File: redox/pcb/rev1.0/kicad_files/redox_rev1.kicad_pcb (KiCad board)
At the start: 2 copper layers, 162.2 x 126.5 mm, 86 parts, among them K0 KEYSW, K1 KEYSW, K10 KEYSW, K11 KEYSW, K12 KEYSW, K13 KEYSW, K14 KEYSW, K15 KEYSW, K16 KEYSW, K2 KEYSW, K20 KEYSW, K21 KEYSW, K22 KEYSW, K23 KEYSW, K24 KEYSW, K25 KEYSW, K26 KEYSW, K3 KEYSW, K30 KEYSW, K31 KEYSW, K32 KEYSW, K33 KEYSW, K34 KEYSW, K35 KEYSW, K36 KEYSW, K4 KEYSW, K40 KEYSW, K41 KEYSW, K42 KEYSW, K43 KEYSW, K44 KEYSW, K45 KEYSW, K46 KEYSW, K5 KEYSW, K6 KEYSW, U1 ProMicro

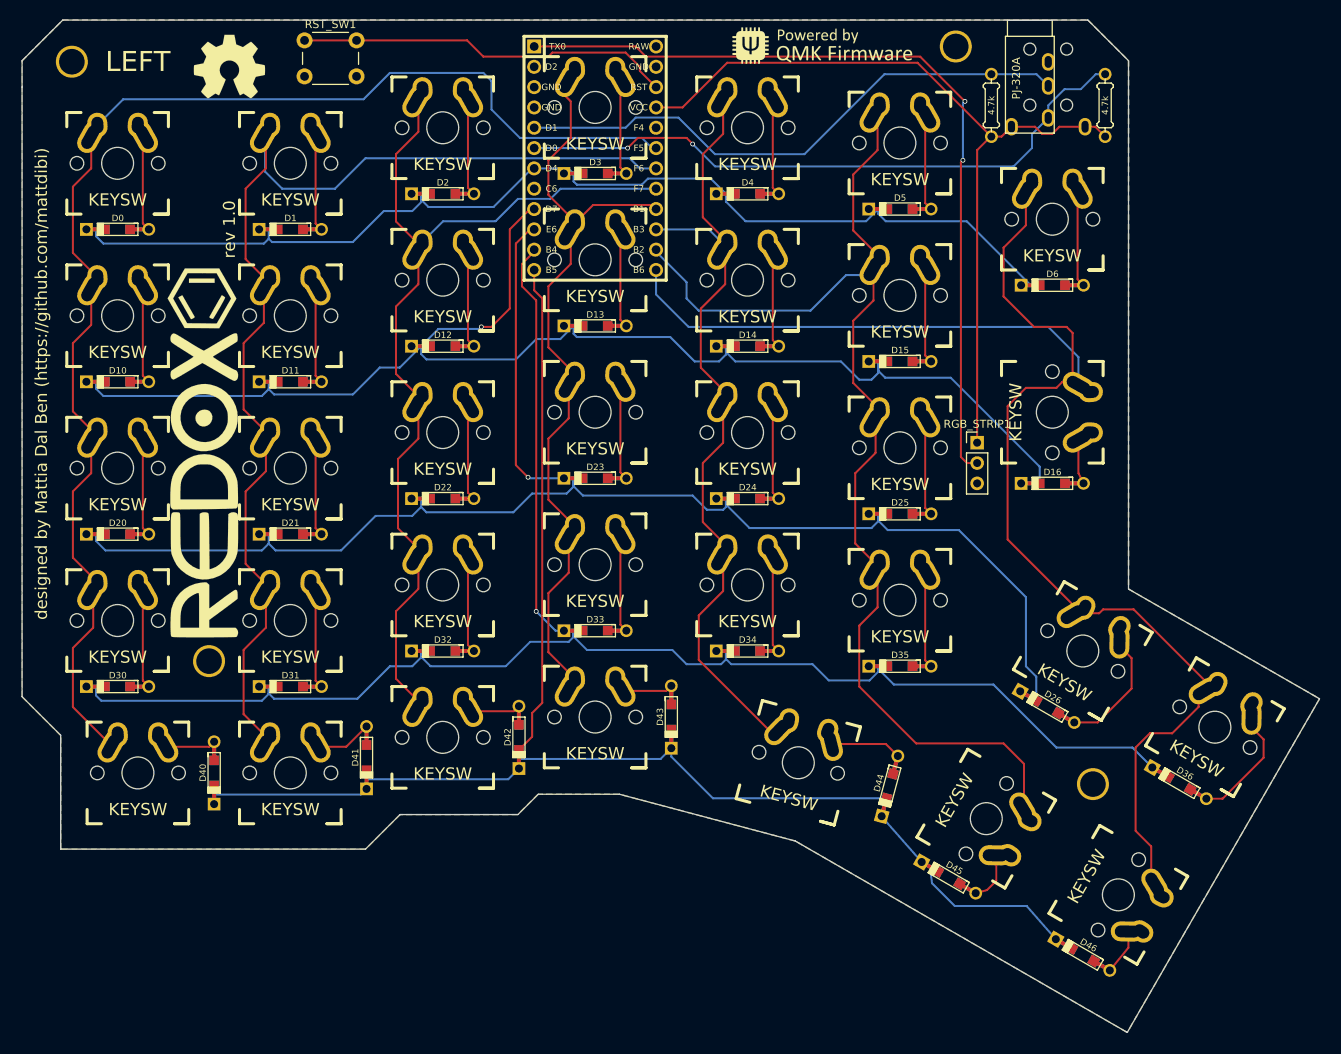
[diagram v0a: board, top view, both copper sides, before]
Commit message: Update to reversible kailh hotswap
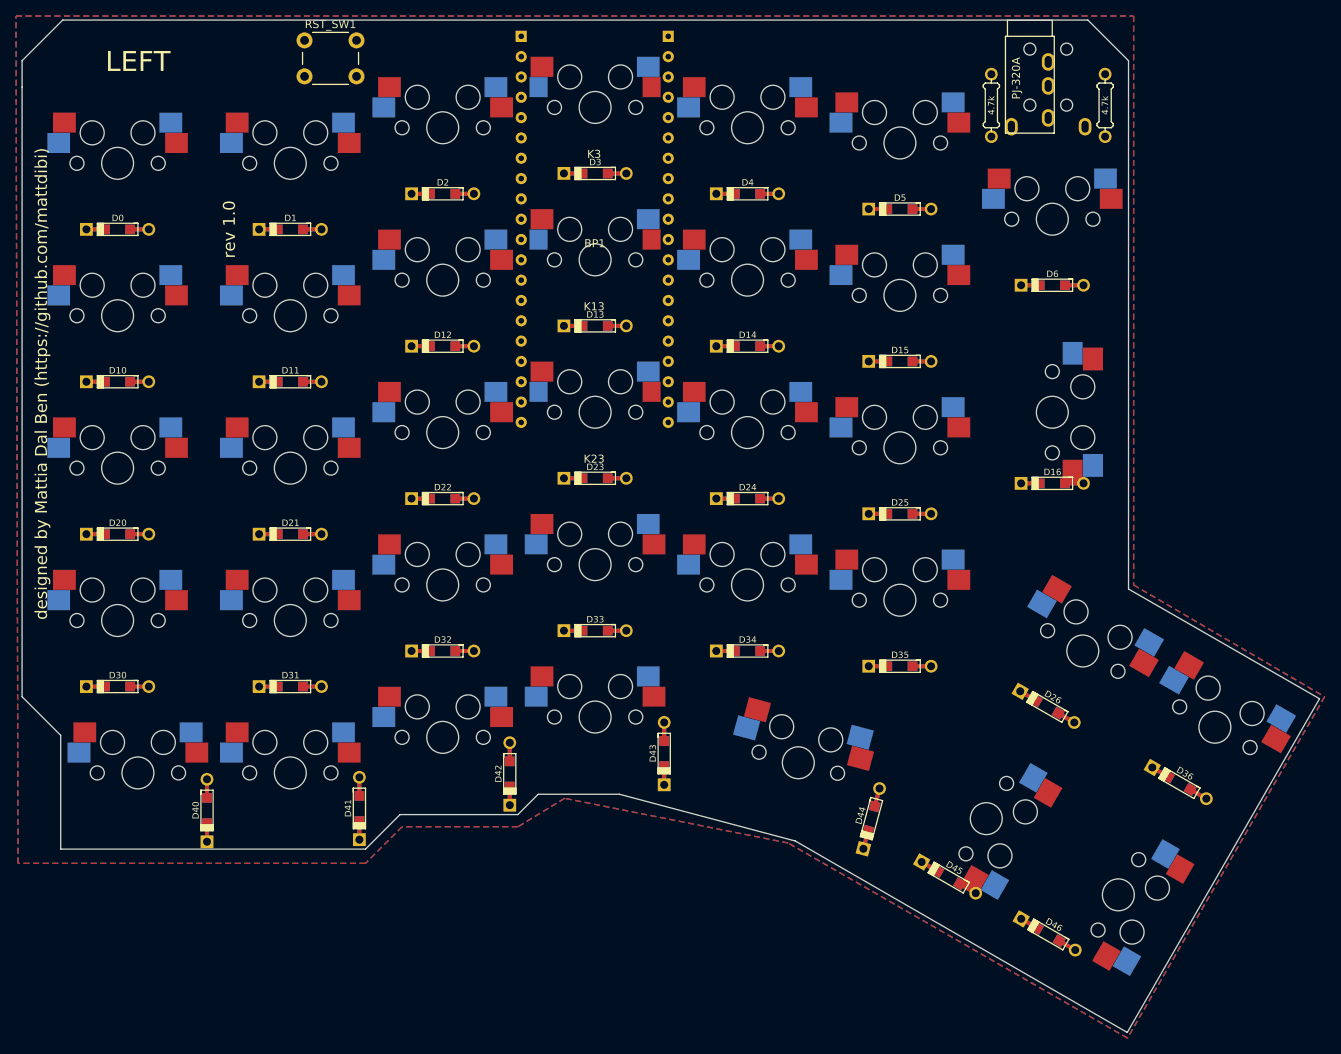
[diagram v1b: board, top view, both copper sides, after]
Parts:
- removed G*** (x2): LOGO, myparts:redox-logo
- removed G*** (x2): LOGO, myparts:qmk-badge
- removed HOLE_M3 (x4): VAL**, keyboard_parts:HOLE_M3
- removed REF*** (x2): OSHW-Logo2_14.6x12mm_SilkScreen, Symbols:OSHW-Symbol_8.9x8mm_SilkScreen
- removed RGB_STRIP1: Conn_01x03, Pin_Headers:Pin_Header_Straight_1x03_Pitch2.54mm
- removed U1: ProMicro, Keebio-Parts:ArduinoProMicro
- added BP1: BlackPill2, reversable_hotswap:BlackPill, F.Cu at (151.1, 76.2)
- K0, K10, K20, K30, K44: footprint myparts:Mx_Alps_125-dualside -> reversable_hotswap:MXOnly-1.25U-Hotswap
- K1, K11, K12, K14, K15, K2, K21, K22, K24, K25, K26, K31, K32, K33, K34, K35, K36, K4, K40, K41, K42, K43, K5, K6: footprint canadian_footprints:Mx_Alps_100-dualside -> reversable_hotswap:MXOnly-1U-Hotswap
- K13, K23, K3: footprint canadian_footprints:Mx_Alps_100-dualside -> reversable_hotswap:MXOnly-1U-Hotswap-Small
- K16, K45, K46: footprint canadian_footprints:Mx_Alps_150-dualsided -> reversable_hotswap:MXOnly-1.5U-Hotswap
- moved D41 6.41 mm to (121.7, 147.3)
- moved D46 5.01 mm to (207.8, 163.1)
- moved D40 4.78 mm to (102.6, 147.6)
- moved D42 4.71 mm to (140.5, 143.0)
- moved D44 4.66 mm to (185.7, 148.6)
- moved D43 4.66 mm to (159.8, 140.5)
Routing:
- net row3: track 207.9 -> 0.00 mm, vias 1 -> 0
- net row4: track 189.3 -> 0.00 mm
- net row2: track 188.9 -> 0.00 mm, vias 1 -> 0
- net col6: track 184.3 -> 0.00 mm
- net row1: track 169.3 -> 0.00 mm, vias 1 -> 0
- net col0: track 167.6 -> 0.00 mm
- net col5: track 146.1 -> 0.00 mm
- net col1: track 144.0 -> 0.00 mm
- net row0: track 135.3 -> 0.00 mm
- net col2: track 119.8 -> 0.00 mm
- net rgb_data: track 103.7 -> 0.00 mm, vias 2 -> 0
- net col4: track 103.1 -> 0.00 mm
- net VCC: track 103.1 -> 0.00 mm
- net col3: track 97.8 -> 0.00 mm
- net SCL: track 80.1 -> 0.00 mm, vias 2 -> 0
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
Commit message: Finish routing and top silkscreen
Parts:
- moved D30 11.4 mm to (102.1, 128.0), turned to 270 degrees
- moved D10 11.3 mm to (102.1, 90.2), turned to 270 degrees
- moved D20 11.2 mm to (101.9, 109.0), turned to 270 degrees
- moved D0 10.9 mm to (101.6, 70.9), turned to 270 degrees
- moved D15 9.91 mm to (198.4, 87.6), turned to 270 degrees
- moved D35 9.88 mm to (198.1, 125.2), turned to 270 degrees
- moved D14 9.71 mm to (178.8, 85.1), turned to 270 degrees
- moved D26 9.58 mm to (217.2, 135.6), turned to 240 degrees
- moved D5 9.54 mm to (197.9, 68.3), turned to 270 degrees
- moved D1 9.54 mm to (121.7, 70.9), turned to 270 degrees
- moved D11 9.54 mm to (121.7, 89.9), turned to 270 degrees
- moved D22 9.52 mm to (141.2, 105.9), turned to 270 degrees
- moved D25 9.44 mm to (197.9, 106.7), turned to 270 degrees
- moved D31 9.44 mm to (121.7, 128.3), turned to 270 degrees
- moved D34 9.39 mm to (178.8, 124.0), turned to 270 degrees
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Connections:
- BP1 pad 21: VCC -> Net-(BP1-Pad21)
- BP1 pad 29: Net-(BP1-Pad29) -> row1
- BP1 pad 32: Net-(BP1-Pad32) -> row0
- BP1 pad 34: row1 -> Net-(BP1-Pad34)
- BP1 pad 36: Net-(BP1-Pad36) -> col3
- BP1 pad 4: col3 -> col4
- BP1 pad 40: row0 -> Net-(BP1-Pad40)
- BP1 pad 5: col4 -> col5
- BP1 pad 6: col5 -> col6
- BP1 pad 7: col6 -> Net-(BP1-Pad7)
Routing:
- net row3: track 0.00 -> 189.4 mm, vias 0 -> 1
- net row4: track 0.00 -> 189.2 mm, vias 0 -> 1
- net row2: track 0.00 -> 185.0 mm, vias 0 -> 1
- net col6: track 0.00 -> 180.2 mm, vias 0 -> 5
- net col0: track 0.00 -> 155.6 mm, vias 0 -> 5
- net col5: track 0.00 -> 139.8 mm, vias 0 -> 5
- net col1: track 0.00 -> 136.9 mm, vias 0 -> 5
- net row1: track 0.00 -> 135.7 mm
- net row0: track 0.00 -> 117.2 mm
- net col2: track 0.00 -> 110.6 mm, vias 0 -> 4
- net col4: track 0.00 -> 100.9 mm, vias 0 -> 5
- net col3: track 0.00 -> 95.8 mm, vias 0 -> 4
- net SCL: track 0.00 -> 93.4 mm, vias 0 -> 1
- net SDA: track 0.00 -> 88.0 mm, vias 0 -> 1
- net RST: track 0.00 -> 84.4 mm
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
